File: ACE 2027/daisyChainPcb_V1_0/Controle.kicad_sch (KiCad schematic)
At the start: 4 parts, among them J1 RJ45, J2 RJ45, J3 Conn_01x02_Pin, J4 Conn_01x02_Pin

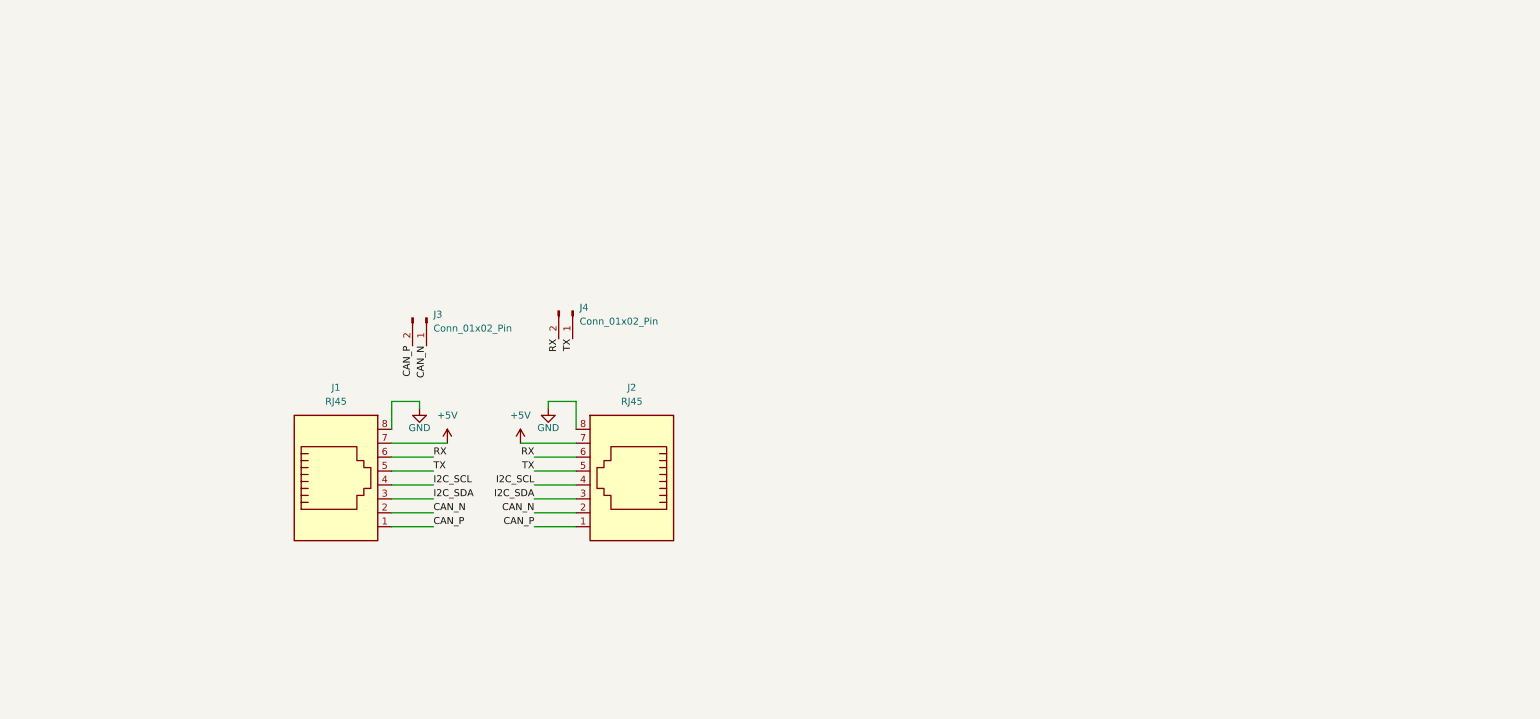
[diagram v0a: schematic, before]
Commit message: Electrical schematic ready for first PR
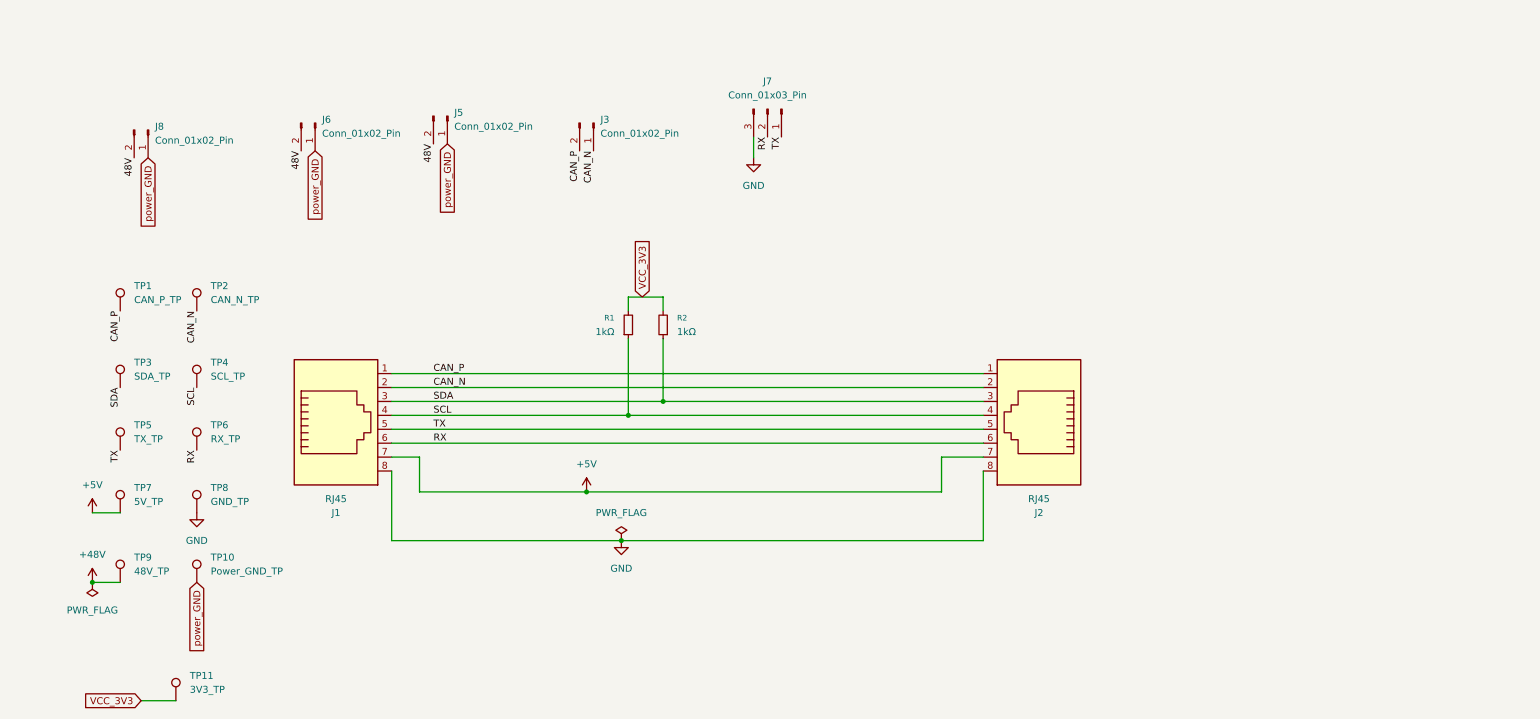
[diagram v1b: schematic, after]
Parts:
- removed J4: Conn_01x02_Pin, symbol Connector:Conn_01x02_Pin
- added J5, J6: Conn_01x02_Pin, Connector_AMASS:AMASS_XT30PW-M_1x02_P2.50mm_Horizontal, symbol Connector:Conn_01x02_Pin
- added J7: Conn_01x03_Pin, daisyChain_Custom:UART_pads, symbol Connector:Conn_01x03_Pin
- added J8: Conn_01x02_Pin, daisyChain_Custom:motorPads, symbol Connector:Conn_01x02_Pin
- added R1, R2: 1kΩ, Resistor_SMD:R_0805_2012Metric_Pad1.20x1.40mm_HandSolder, symbol Device:R_Small
- added TP1: CAN_P_TP, TestPoint:TestPoint_Pad_D2.0mm, symbol Connector:TestPoint
- added TP10: Power_GND_TP, TestPoint:TestPoint_Pad_D2.0mm, symbol Connector:TestPoint
- added TP11: 3V3_TP, TestPoint:TestPoint_Pad_D2.0mm, symbol Connector:TestPoint
- added TP2: CAN_N_TP, TestPoint:TestPoint_Pad_D2.0mm, symbol Connector:TestPoint
- added TP3: SDA_TP, TestPoint:TestPoint_Pad_D2.0mm, symbol Connector:TestPoint
- added TP4: SCL_TP, TestPoint:TestPoint_Pad_D2.0mm, symbol Connector:TestPoint
- added TP5: TX_TP, TestPoint:TestPoint_Pad_D2.0mm, symbol Connector:TestPoint
- added TP6: RX_TP, TestPoint:TestPoint_Pad_D2.0mm, symbol Connector:TestPoint
- added TP7: 5V_TP, TestPoint:TestPoint_Pad_D2.0mm, symbol Connector:TestPoint
- added TP8: GND_TP, TestPoint:TestPoint_Pad_D2.0mm, symbol Connector:TestPoint
- added TP9: 48V_TP, TestPoint:TestPoint_Pad_D2.0mm, symbol Connector:TestPoint
- J1, J2: footprint (none) -> Connector_RJ:RJ45_Amphenol_54602-x08_Horizontal
- J3: footprint (none) -> daisyChain_Custom:CAN_pads
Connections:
- net +5V: now also TP7.1
- net CAN_N: now also TP2.1
- net CAN_P: now also TP1.1
- net GND: now also J7.3 (Pin_3), TP8.1
- net RX: now also J7.2 (Pin_2), TP6.1
- net TX: now also J7.1 (Pin_1), TP5.1
- net I2C_SCL renamed SCL
- net SCL: now also R1.1, TP4.1
- net I2C_SDA renamed SDA
- net SDA: now also R2.1, TP3.1
- new net +48V: TP9.1
- new net 48V: J5.2 (Pin_2), J6.2 (Pin_2), J8.2 (Pin_2)
- new net VCC_3V3: R1.2, R2.2, TP11.1
- new net power_GND: J5.1 (Pin_1), J6.1 (Pin_1), J8.1 (Pin_1), TP10.1
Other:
- moved on the sheet: J1, J2, J3

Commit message: Schematic PR fix - Separated schematic sections into blocs - Indicated the connector type in the name - Added datasheets for the connectors
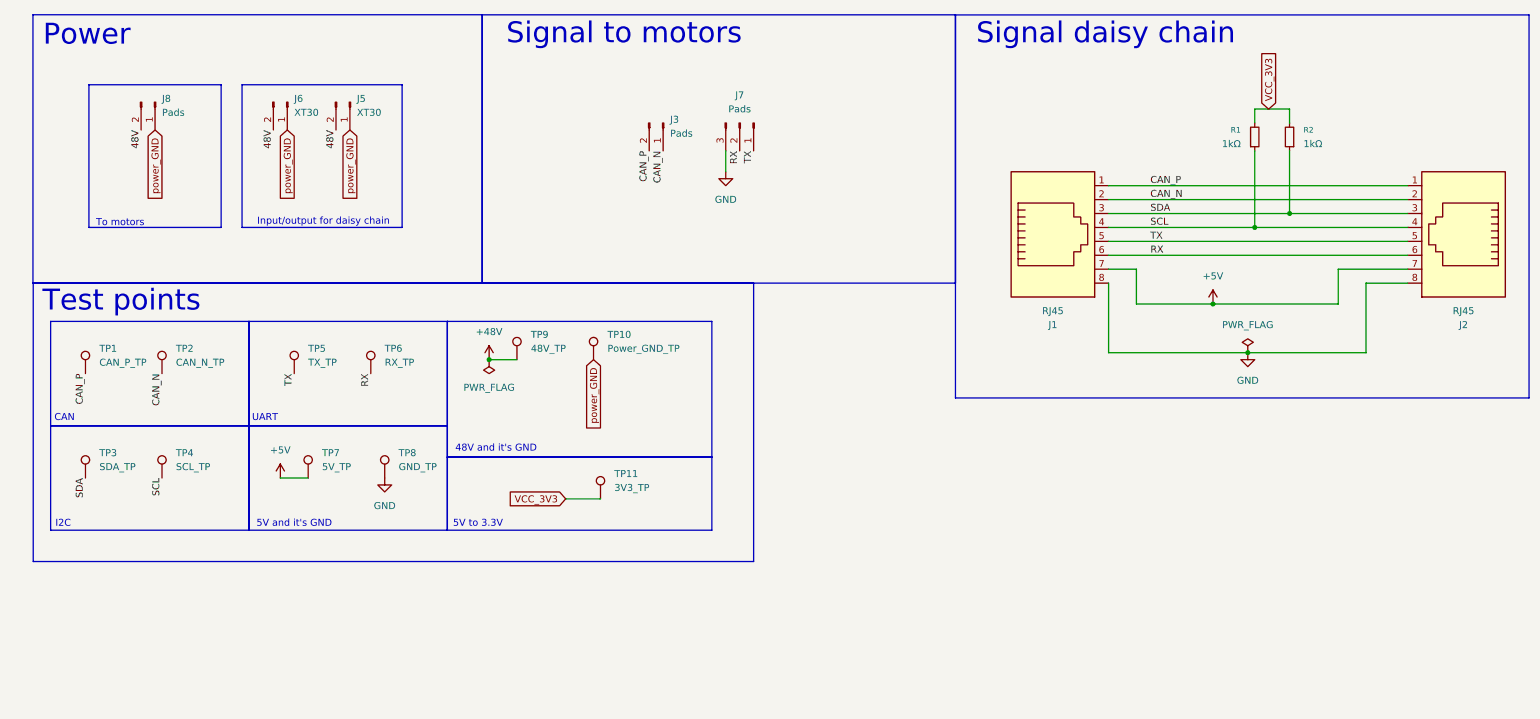
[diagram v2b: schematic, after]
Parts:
- J3, J8: value Conn_01x02_Pin -> Pads
- J5, J6: value Conn_01x02_Pin -> XT30
- J7: value Conn_01x03_Pin -> Pads
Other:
- note added: "48V and it's GND"
- note added: "5V and it's GND"
- note added: "5V to 3.3V"
- note added: "CAN"
- note added: "I2C"
- note added: "Input/output for daisy chain"
- note added: "Power"
- note added: "Signal daisy chain"
- note added: "Signal to motors"
- note added: "Test points"
- note added: "To motors"
- note added: "UART"
- moved on the sheet: J1, J2, J3, J5, J6, J7, J8, R1, R2, TP1, TP10, TP11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

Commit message: Added datasheet for the RJ45 connectors
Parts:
- J1, J2: Digi-Key_PN (none) -> 609-1046-ND
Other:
- note added: "48V and its GND"
- note added: "5V and its GND"
- note removed: "48V and it's GND"
- note removed: "5V and it's GND"
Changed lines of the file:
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@@
 		)
 	)
-	(text "48V and it's GND"
+	(text "48V and its GND"
 		(exclude_from_sim no)
 		(at 96.52 91.186 0)
@@
 		)
 	)
-	(text "5V and it's GND"
+	(text "5V and its GND"
 		(exclude_from_sim no)
 		(at 59.69 104.902 0)
@@
 			)
 		)
-		(property "Datasheet" ""
+		(property "Datasheet" "https://www.waldom.com/upload/parts/datasheets/mf-fci/fci-54602-908lf.pdf"
 			(at 198.12 51.435 90)
 			(hide yes)
@@
 		)
 		(property "Description" "RJ connector, 8P8C (8 positions 8 connected)"
+			(at 198.12 50.8 0)
+			(hide yes)
+			(show_name no)
+			(do_not_autoplace no)
+			(effects
+				(font
+					(size 1.27 1.27)
+				)
+			)
+		)
+		(property "Digi-Key_PN" "609-1046-ND"
 			(at 198.12 50.8 0)
 			(hide yes)
@@
 			)
 		)
-		(property "Datasheet" ""
+		(property "Datasheet" "https://www.waldom.com/upload/parts/datasheets/mf-fci/fci-54602-908lf.pdf"
 			(at 273.05 51.435 90)
 			(hide yes)
@@
 			(at 273.05 50.8 0)
 			(hide yes)
+			(show_name no)
+			(do_not_autoplace no)
+			(effects
+				(font
+					(size 1.27 1.27)
+				)
+			)
+		)
+		(property "Digi-Key_PN" "609-1046-ND"
+			(at 273.05 50.8 0)
+			(hide yes)

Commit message: Updated grounds to reflect the two grounds we have
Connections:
- net GND renamed signal_GND
